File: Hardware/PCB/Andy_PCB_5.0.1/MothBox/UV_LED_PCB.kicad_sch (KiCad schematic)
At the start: 16 parts, among them P4 External Attractor, Q4 YJQ10N2A, Q5 YJQ10N2A, Q6 YJQ10N2A, Q7 YJQ10N2A

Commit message: updated photo LEDs and the power page
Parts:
- removed A1, A2, A3: PZ254R-11-04P, easyeda2kicad:HDR-TH_4P-P2.54-H-M-W10.4, symbol MB_Library:PZ254R-11-04P
- added H10, H8, H9: PZ254R-12-8P, easyeda2kicad:HDR-TH_8P-P2.54-H-M-R2-C4-S2.54, symbol easyeda_libraries:PZ254R-12-8P
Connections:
- net +12V: now also H10.1, H10.3, H8.1, H8.3, H9.1, H9.3
- net at Q6.1 (D), Q6.2 (D), Q6.3 (D)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: now also H8.5, H8.7
- net at Q5.1 (D), Q5.2 (D), Q5.3 (D)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: now also H10.5, H10.7
- net at Q7.1 (D), Q7.2 (D), Q7.3 (D)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: now also H9.5, H9.7
- no-connect marks 0 -> 12
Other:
- note added: "v5.0.0 used the: PZ254R-11-04P single row connector"
- company: (none) -> Digital Naturalism Laboritories
- title: (none) -> MothBox

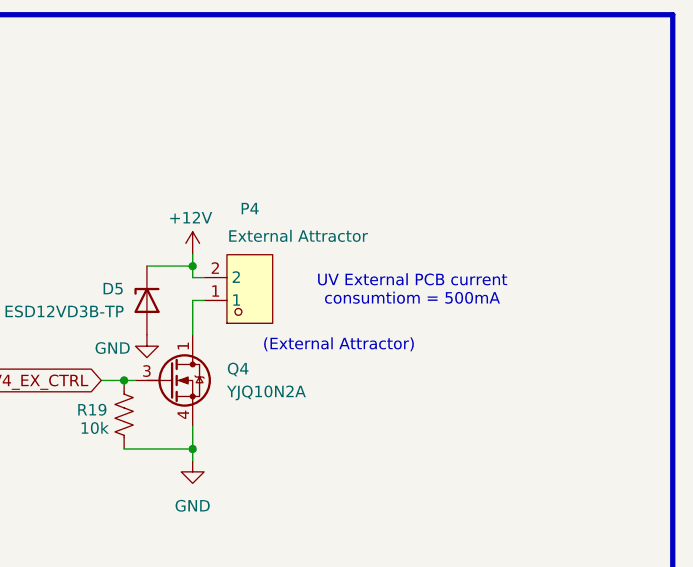
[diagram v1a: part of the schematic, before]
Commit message: updated footprints and schematic
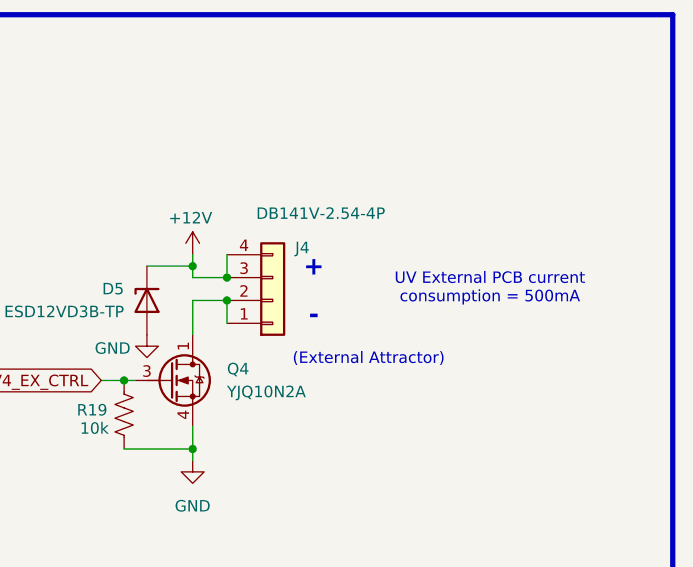
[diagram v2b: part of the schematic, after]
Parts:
- removed P4: External Attractor, easyeda2kicad:CONN-TH_2P-P5.08_DIBO_DB142R-5.08-2P, symbol MB_Library:DB142R-5.08-2P
- added J4: DB141V-2.54-4P, easyeda_footprints:CONN-TH_4P-P2.54_DIBO_DB141V-2.54-4P, symbol MothBox_Symbol_Library:Conn_01x04
- D2, D5, D6, D7: symbol MB_Library:ESD5Zxx -> MothBox_Symbol_Library:ESD5Zxx; LCSC Part no  C435886 -> (none); LCSC_Part_No (none) -> C435886
- H10, H8, H9: footprint easyeda2kicad:HDR-TH_8P-P2.54-H-M-R2-C4-S2.54 -> easyeda_footprints:HDR-TH_8P-P2.54-H-M-R2-C4-S2.54; symbol easyeda_libraries:PZ254R-12-8P -> MothBox_Symbol_Library:PZ254R-12-8P; LCSC Part C492432 -> (none); LCSC_Part (none) -> C492432
- Q4: footprint Pauls_Footprints:DFN2020-3 -> pauls_footprints:DFN2020-3; symbol _pauls_library:YJQ10N2A -> MothBox_Symbol_Library:YJQ10N2A_1_1_1
- Q5: footprint Pauls_Footprints:DFN2020-3 -> pauls_footprints:DFN2020-3; symbol _pauls_library:YJQ10N2A -> MothBox_Symbol_Library:YJQ10N2A_2_1_1
- Q6: footprint Pauls_Footprints:DFN2020-3 -> pauls_footprints:DFN2020-3; symbol _pauls_library:YJQ10N2A -> MothBox_Symbol_Library:YJQ10N2A_3_1_1
- Q7: footprint Pauls_Footprints:DFN2020-3 -> pauls_footprints:DFN2020-3; symbol _pauls_library:YJQ10N2A -> MothBox_Symbol_Library:YJQ10N2A_4_1_1
- R19, R21, R27, R28: symbol MB_Library:R_US -> MothBox_Symbol_Library:R_US; LCSC Part no  C84376 -> (none); LCSC_Part_No (none) -> C84376
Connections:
- net +12V: now also J4.3 (Pin_3), J4.4 (Pin_4)
- net at Q4.1 (D), Q4.2 (D), Q4.3 (D)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: now also J4.1 (Pin_1), J4.2 (Pin_2)
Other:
- note added: "+"
- note added: "-"
- note added: "UV External PCB current consumption = 500mA"
- note removed: "UV External PCB current consumtiom = 500mA"

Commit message: daily PCB update
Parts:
- D2, D5, D6, D7: footprint Diode_SMD:D_SOD-323 -> MothBox_footprints_Library:D_SOD-323
- H10, H8, H9: footprint easyeda_footprints:HDR-TH_8P-P2.54-H-M-R2-C4-S2.54 -> MothBox_footprints_Library:HDR-TH_8P-P2.54-H-M-R2-C4-S2.54
- J4: footprint easyeda_footprints:CONN-TH_4P-P2.54_DIBO_DB141V-2.54-4P -> MothBox_footprints_Library:CONN-TH_4P-P2.54_DIBO_DB141V-2.54-4P
- Q4: footprint pauls_footprints:DFN2020-3 -> MothBox_footprints_Library:DFN2020-3; symbol MothBox_Symbol_Library:YJQ10N2A_1_1_1 -> MothBox_Symbol_Library:YJQ10N2A_1_1_1_1_1
- Q5: footprint pauls_footprints:DFN2020-3 -> MothBox_footprints_Library:DFN2020-3; symbol MothBox_Symbol_Library:YJQ10N2A_2_1_1 -> MothBox_Symbol_Library:YJQ10N2A_2_1_1_1_1
- Q6: footprint pauls_footprints:DFN2020-3 -> MothBox_footprints_Library:DFN2020-3; symbol MothBox_Symbol_Library:YJQ10N2A_3_1_1 -> MothBox_Symbol_Library:YJQ10N2A_3_1_1_1_1
- Q7: footprint pauls_footprints:DFN2020-3 -> MothBox_footprints_Library:DFN2020-3; symbol MothBox_Symbol_Library:YJQ10N2A_4_1_1 -> MothBox_Symbol_Library:YJQ10N2A_4_1_1_1_1
- R19, R21, R27, R28: footprint Resistor_SMD:R_0805_2012Metric -> MothBox_footprints_Library:R_0805_2012Metric
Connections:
- net +12V: now also H8.2, H8.4, H9.2, H9.4; no longer H8.1, H8.3, H9.1, H9.3
- net at Q7.1 (D), Q7.2 (D), Q7.3 (D)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: now also H9.6, H9.8; no longer H9.5, H9.7
- net at Q6.1 (D), Q6.2 (D), Q6.3 (D)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: now also H8.6, H8.8; no longer H8.5, H8.7

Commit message: rough outline of PCB. Lots of tidying up needed
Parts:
- removed Q4: YJQ10N2A, MothBox_footprints_Library:DFN2020-3, symbol MothBox_Symbol_Library:YJQ10N2A_1_1_1_1_1
- removed Q5: YJQ10N2A, MothBox_footprints_Library:DFN2020-3, symbol MothBox_Symbol_Library:YJQ10N2A_2_1_1_1_1
- removed Q6: YJQ10N2A, MothBox_footprints_Library:DFN2020-3, symbol MothBox_Symbol_Library:YJQ10N2A_3_1_1_1_1
- removed Q7: YJQ10N2A, MothBox_footprints_Library:DFN2020-3, symbol MothBox_Symbol_Library:YJQ10N2A_4_1_1_1_1
- removed R19, R21, R27, R28: 10k, MothBox_footprints_Library:R_0805_2012Metric, symbol MothBox_Symbol_Library:R_US
- added Q4, Q5, Q6, Q9: YJQ10N2A, MothBox_footprints_Library:U-DFN2020-6_L2.0-W2.0-P0.65-BL, symbol MothBox_Symbol_Library:YJQ10N2A_1
- added R19, R21, R27, R31: 10K, MothBox_footprints_Library:R_0603_1608Metric, symbol MothBox_Symbol_Library:R_Small
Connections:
- net +12V: now also H10.2, H10.4; no longer H10.1, H10.3
- net GND: now also Q4.4 (S), Q4.7 (S), Q5.4 (S), Q5.7 (S), Q6.4 (S), Q6.7 (S), Q9.4 (S), Q9.7 (S), R19.2, R21.2, R27.2, R31.2
- net UV1_CTRL: now also Q5.3 (G), R27.1
- net UV2_CTRL: now also Q9.3 (G), R21.1
- net UV3_CTRL: now also Q6.3 (G), R31.1
- net UV4_EX_CTRL: now also Q4.3 (G), R19.1
- net at J4.1 (Pin_1), J4.2 (Pin_2): now also Q4.1 (D), Q4.2 (D), Q4.5 (D), Q4.6 (D), Q4.8 (D)
- net at H10.5: no longer H10.7
- net at H10.6: now also H10.8, Q9.1 (D), Q9.2 (D), Q9.5 (D), Q9.6 (D), Q9.8 (D)
- net at H9.6, H9.8: now also Q6.1 (D), Q6.2 (D), Q6.5 (D), Q6.6 (D), Q6.8 (D)
- net at H8.6, H8.8: now also Q5.1 (D), Q5.2 (D), Q5.5 (D), Q5.6 (D), Q5.8 (D)

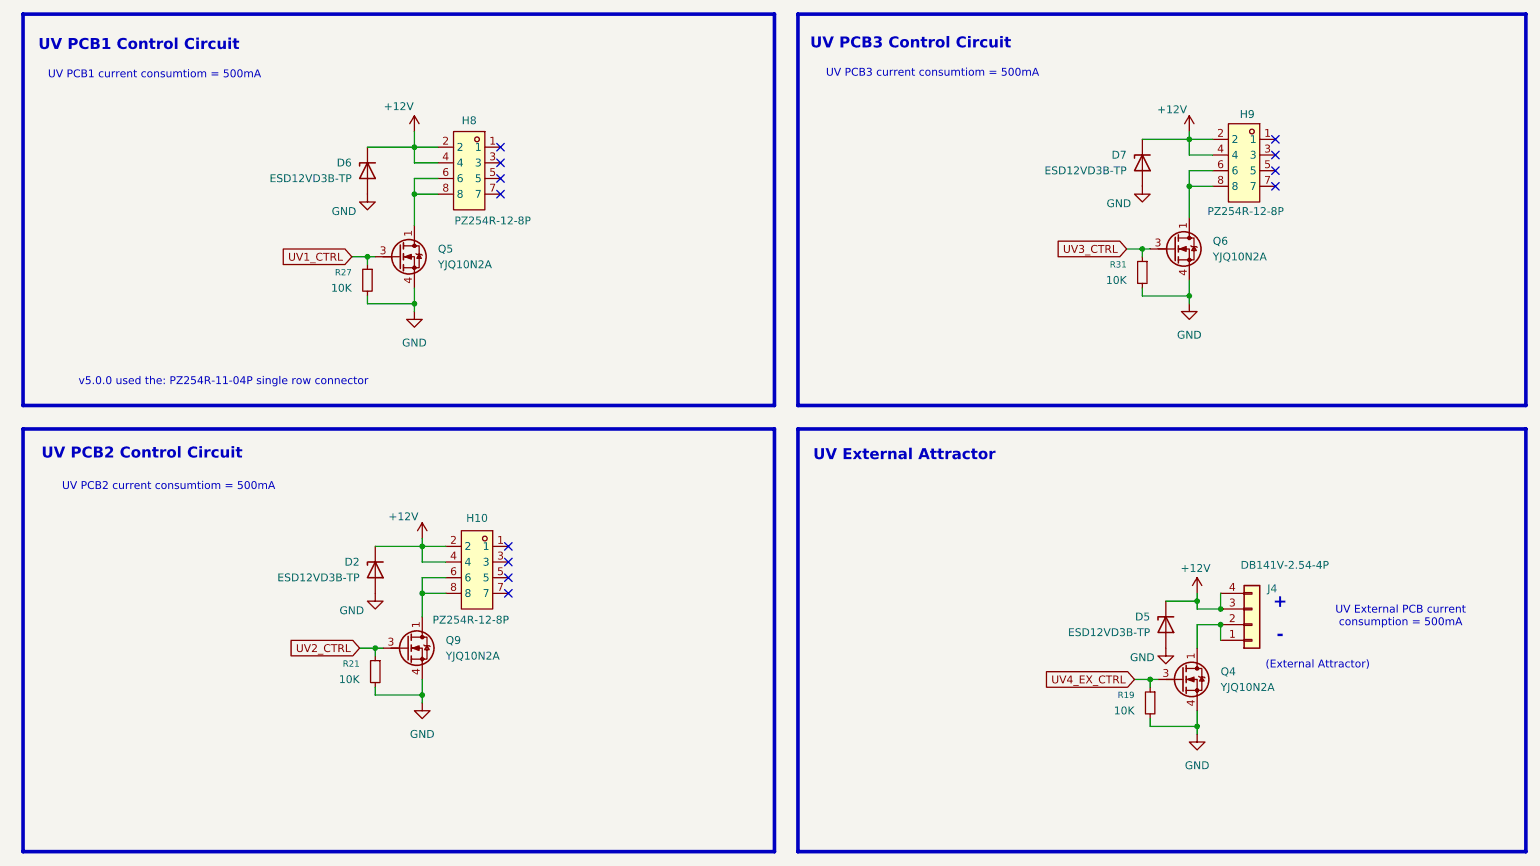
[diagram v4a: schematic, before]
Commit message: updated MothBeam PCB Edge and MothBox PCB
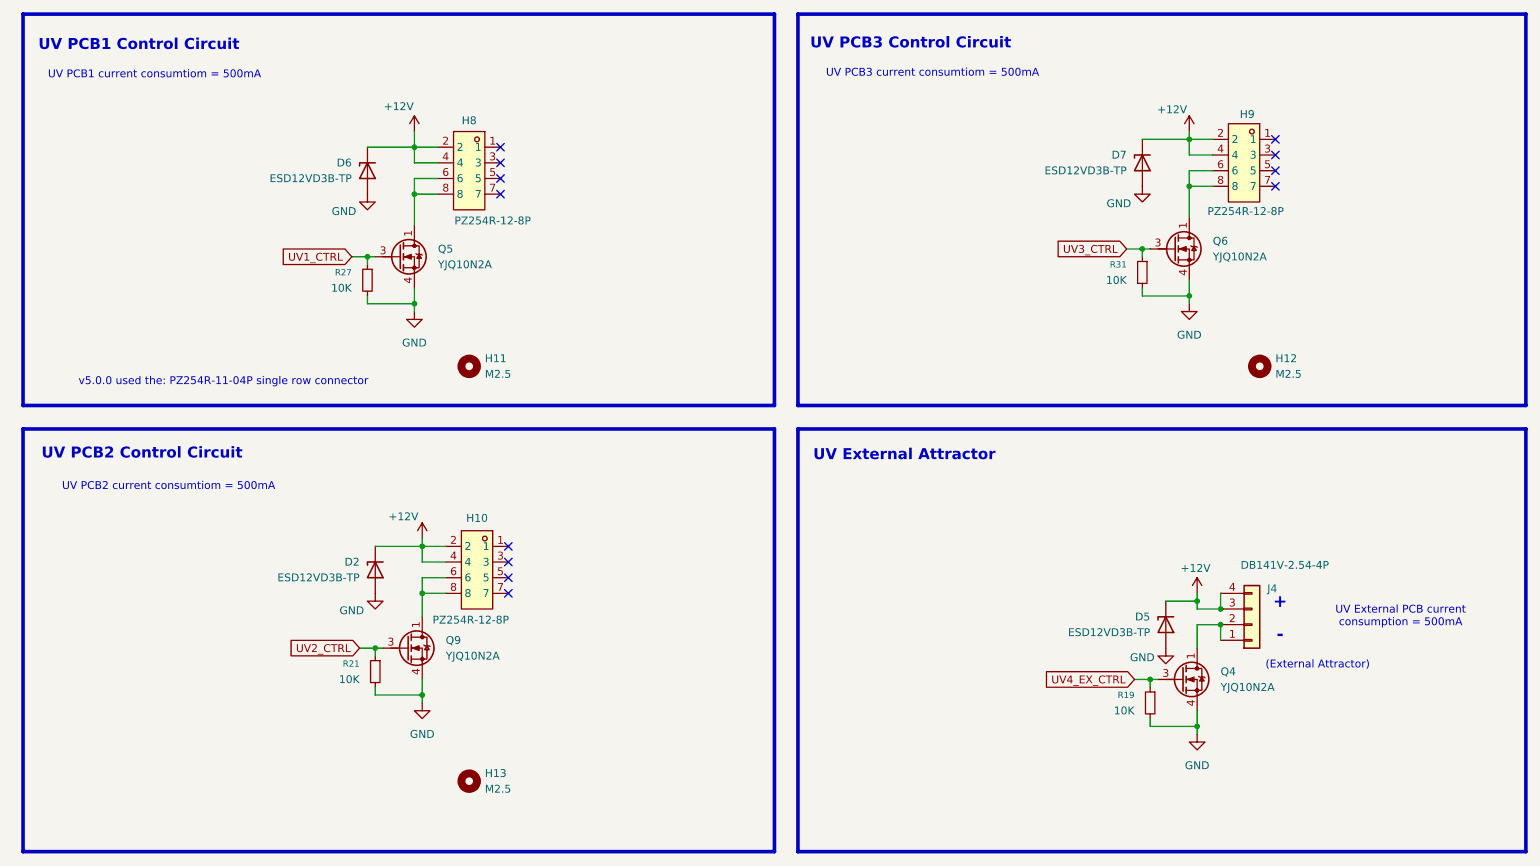
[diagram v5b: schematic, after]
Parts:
- added H11, H12, H13: M2.5, MountingHole:MountingHole_2.7mm, symbol Mechanical:MountingHole
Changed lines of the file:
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@@
+	)
+	(symbol
+		(lib_id "Mechanical:MountingHole")
+		(at 227.33 85.09 0)
+		(unit 1)
+		(exclude_from_sim no)
+		(in_bom no)
+		(on_board yes)
+		(dnp no)
+		(fields_autoplaced yes)
+		(property "Reference" "H12"
+			(at 229.87 83.8199 0)
+			(effects
+				(font
+					(size 1.27 1.27)
+				)
+				(justify left)
+			)
+		)
+		(property "Value" "M2.5"
+			(at 229.87 86.3599 0)
+			(effects
+				(font
+					(size 1.27 1.27)
+				)
+				(justify left)
+			)
+		)
+		(property "Footprint" "MountingHole:MountingHole_2.7mm"
+			(at 227.33 85.09 0)
+			(effects
+				(font
+					(size 1.27 1.27)
+				)
+				(hide yes)
+			)
+		)
+		(property "Datasheet" "~"
+			(at 227.33 85.09 0)
+			(effects
+				(font
+					(size 1.27 1.27)
+				)
+				(hide yes)
+			)
+		)
+		(property "Description" "Mounting Hole without connection"
+			(at 227.33 85.09 0)
+			(effects
+				(font
+					(size 1.27 1.27)
+				)
+				(hide yes)
+			)
+		)
+		(instances
+			(project "MothBox"
+				(path "/9021e528-fc76-4423-a3f3-30f5652071cc/25f161be-2136-4f06-bcb6-1cc6303e8ec0"
+					(reference "H12")
+					(unit 1)
+				)
+			)
+		)
 	)
 	(symbol
@@
 	)
 	(symbol
+		(lib_id "Mechanical:MountingHole")
+		(at 99.06 152.4 0)
+		(unit 1)
+		(exclude_from_sim no)
+		(in_bom no)
+		(on_board yes)
+		(dnp no)
+		(fields_autoplaced yes)
+		(property "Reference" "H13"
+			(at 101.6 151.1299 0)
+			(effects
+				(font
+					(size 1.27 1.27)
+				)
+				(justify left)
+			)
+		)
+		(property "Value" "M2.5"
+			(at 101.6 153.6699 0)
+			(effects
+				(font
+					(size 1.27 1.27)
+				)
+				(justify left)
+			)
+		)
+		(property "Footprint" "MountingHole:MountingHole_2.7mm"
+			(at 99.06 152.4 0)
+			(effects
+				(font
+					(size 1.27 1.27)
+				)
+				(hide yes)
+			)
+		)
+		(property "Datasheet" "~"
+			(at 99.06 152.4 0)
+			(effects
+				(font
+					(size 1.27 1.27)
+				)
+				(hide yes)
+			)
+		)
+		(property "Description" "Mounting Hole without connection"
+			(at 99.06 152.4 0)
+			(effects
+				(font
+					(size 1.27 1.27)
+				)
+				(hide yes)
+			)
+		)
+		(instances
+			(project "MothBox"
+				(path "/9021e528-fc76-4423-a3f3-30f5652071cc/25f161be-2136-4f06-bcb6-1cc6303e8ec0"
+					(reference "H13")
+					(unit 1)
+				)
+			)
+		)
+	)
+	(symbol
 		(lib_id "MothBox_Symbol_Library:GND")
 		(at 91.44 139.7 0)
@@
 					(unit 1)
 				)
+			)
+		)
+	)
+	(symbol
+		(lib_id "Mechanical:MountingHole")
+		(at 99.06 85.09 0)
+		(unit 1)
+		(exclude_from_sim no)
+		(in_bom no)
+		(on_board yes)
+		(dnp no)
+		(fields_autoplaced yes)
+		(property "Reference" "H11"
+			(at 101.6 83.8199 0)
+			(effects
+				(font
+					(size 1.27 1.27)
+				)
+				(justify left)
+			)
+		)
+		(property "Value" "M2.5"
+			(at 101.6 86.3599 0)
+			(effects
+				(font
+					(size 1.27 1.27)
+				)
+				(justify left)
+			)
+		)
+		(property "Footprint" "MountingHole:MountingHole_2.7mm"
+			(at 99.06 85.09 0)
+			(effects
+				(font
+					(size 1.27 1.27)
+				)
+				(hide yes)
+			)
+		)
+		(property "Datasheet" "~"
+			(at 99.06 85.09 0)
+			(effects
+				(font
+					(size 1.27 1.27)
+				)
+				(hide yes)
+			)
+		)
+		(property "Description" "Mounting Hole without connection"
+			(at 99.06 85.09 0)
+			(effects
+				(font
+					(size 1.27 1.27)
+				)
+				(hide yes)
+			)
+		)
+		(instances
+			(project ""
+				(path "/9021e528-fc76-4423-a3f3-30f5652071cc/25f161be-2136-4f06-bcb6-1cc6303e8ec0"
+					(reference "H11")
+					(unit 1)
+				)

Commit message: added in extra hour switch for 24hr coverage
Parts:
- D2, D5, D6, D7: LCSC_Part (none) -> C435886; LCSC_Part_No C435886 -> (none)
- J4: LCSC C2898746 -> (none); LCSC_Part (none) -> C2898746
- Q4, Q5, Q6, Q9: LCSC C919558 -> (none); LCSC_Part (none) -> C919558
- R19, R21, R27, R31: LCSC_Part (none) -> C25804
